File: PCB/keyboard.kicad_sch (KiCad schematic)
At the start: 0 parts

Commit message: created MCU schematic
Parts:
- added C? (x3): 0.1uF, symbol Device:C_Small
- added C? (x2): 22pF, symbol Device:C_Small
- added C?: 1uf, symbol Device:C_Small
- added C?: 10uF, symbol Device:C_Small
- added R? (x2): 10k, symbol Device:R_Small
- added R? (x2): 22, symbol Device:R_Small
- added SW?: SW_Push, symbol Switch:SW_Push
- added U?: ATmega32U4-A, Package_QFP:TQFP-44_10x10mm_P0.8mm, symbol MCU_Microchip_ATmega:ATmega32U4-A
- added Y?: 16MHz, symbol Device:Crystal_GND24_Small
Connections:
- new net: C?.2, U?.17 (XTAL1), Y?.1
- new net: R?.2, SW?.2, U?.13 (~{RESET})
- new net: C?.2, U?.16 (XTAL2), Y?.3
- new net: R?.2, U?.3 (D-)
- new net: R?.1, U?.33 (~{HWB}/PE2)
- new net: R?.2, U?.4 (D+)
- new net: C?.1, U?.6 (UCAP)
- new net +5V: C?.1, C?.1, C?.1, C?.1, R?.1, U?.14 (VCC), U?.2 (UVCC), U?.24 (AVCC), U?.34 (VCC), U?.44 (AVCC), U?.7 (VBUS)
- new net D +: R?.1
- new net D -: R?.1
- new net GND: C?.1, C?.1, C?.2, C?.2, C?.2, C?.2, C?.2, R?.2, SW?.1, U?.15 (GND), U?.23 (GND), U?.35 (GND), U?.43 (GND), U?.5 (UGND), Y?.2, Y?.4
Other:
- note added: "1"
- note added: "22/10/22"
- note added: "Smth66"

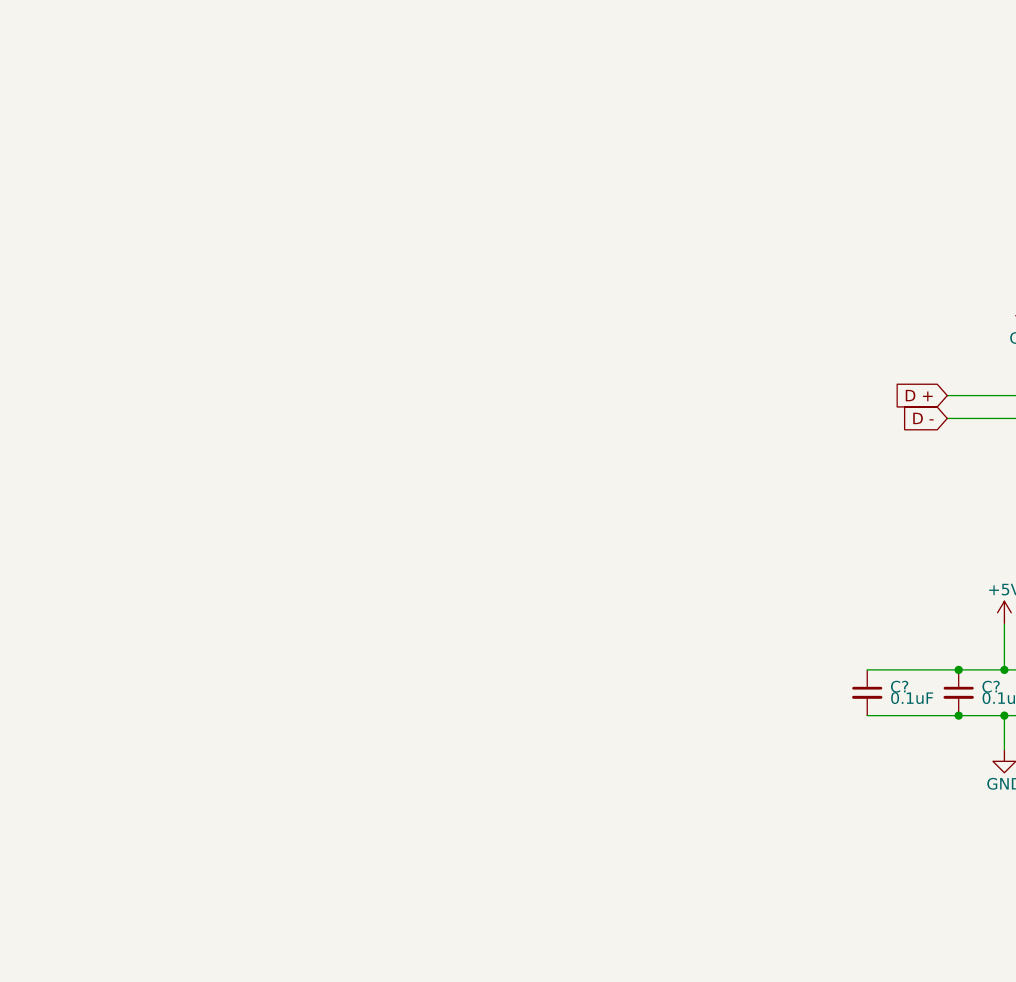
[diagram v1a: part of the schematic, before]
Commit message: added USB and Switch to schematic
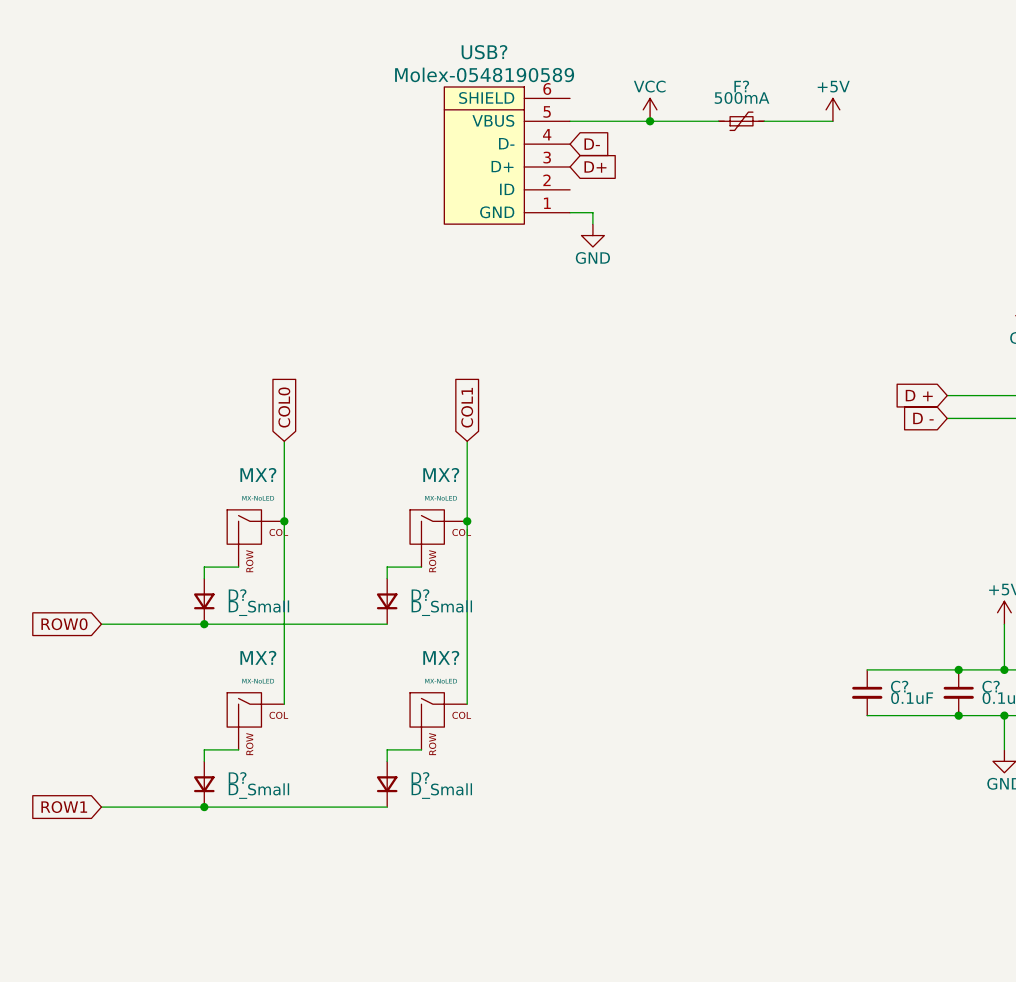
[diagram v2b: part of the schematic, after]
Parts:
- added D? (x4): D_Small, symbol Device:D_Small
- added F?: 500mA, symbol Device:Polyfuse_Small
- added MX? (x4): MX-NoLED, symbol MX_Alps_Hybrid:MX-NoLED
- added USB?: Molex-0548190589, symbol random-keyboard-parts:Molex-0548190589
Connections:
- net +5V: now also F?.2
- net GND: now also USB?.1 (GND)
- new net: D?.2 (A), MX?.2 (ROW) (x4)
- new net COL0: MX?.1 (COL), MX?.1 (COL)
- new net COL1: MX?.1 (COL), MX?.1 (COL)
- new net D+: USB?.3 (D+)
- new net D-: USB?.4 (D-)
- new net ROW0: D?.1 (K), D?.1 (K)
- new net ROW1: D?.1 (K), D?.1 (K)
- new net VCC: F?.1, USB?.5 (VBUS)

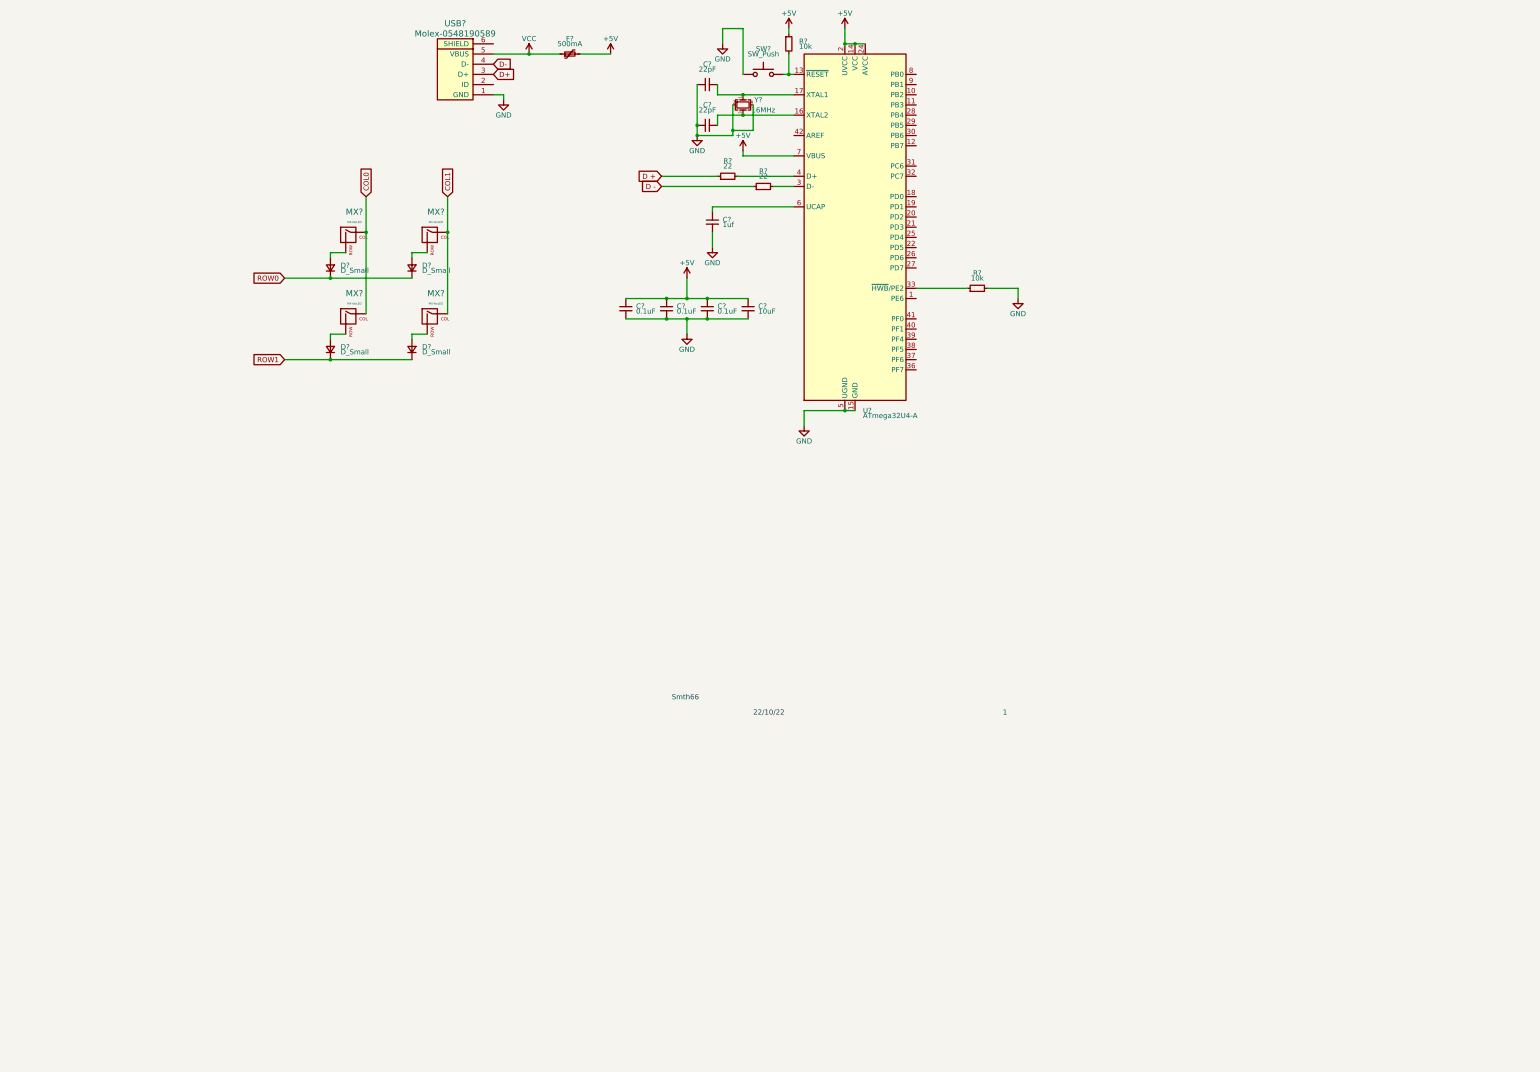
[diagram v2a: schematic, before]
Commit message: added switch grid to schematic
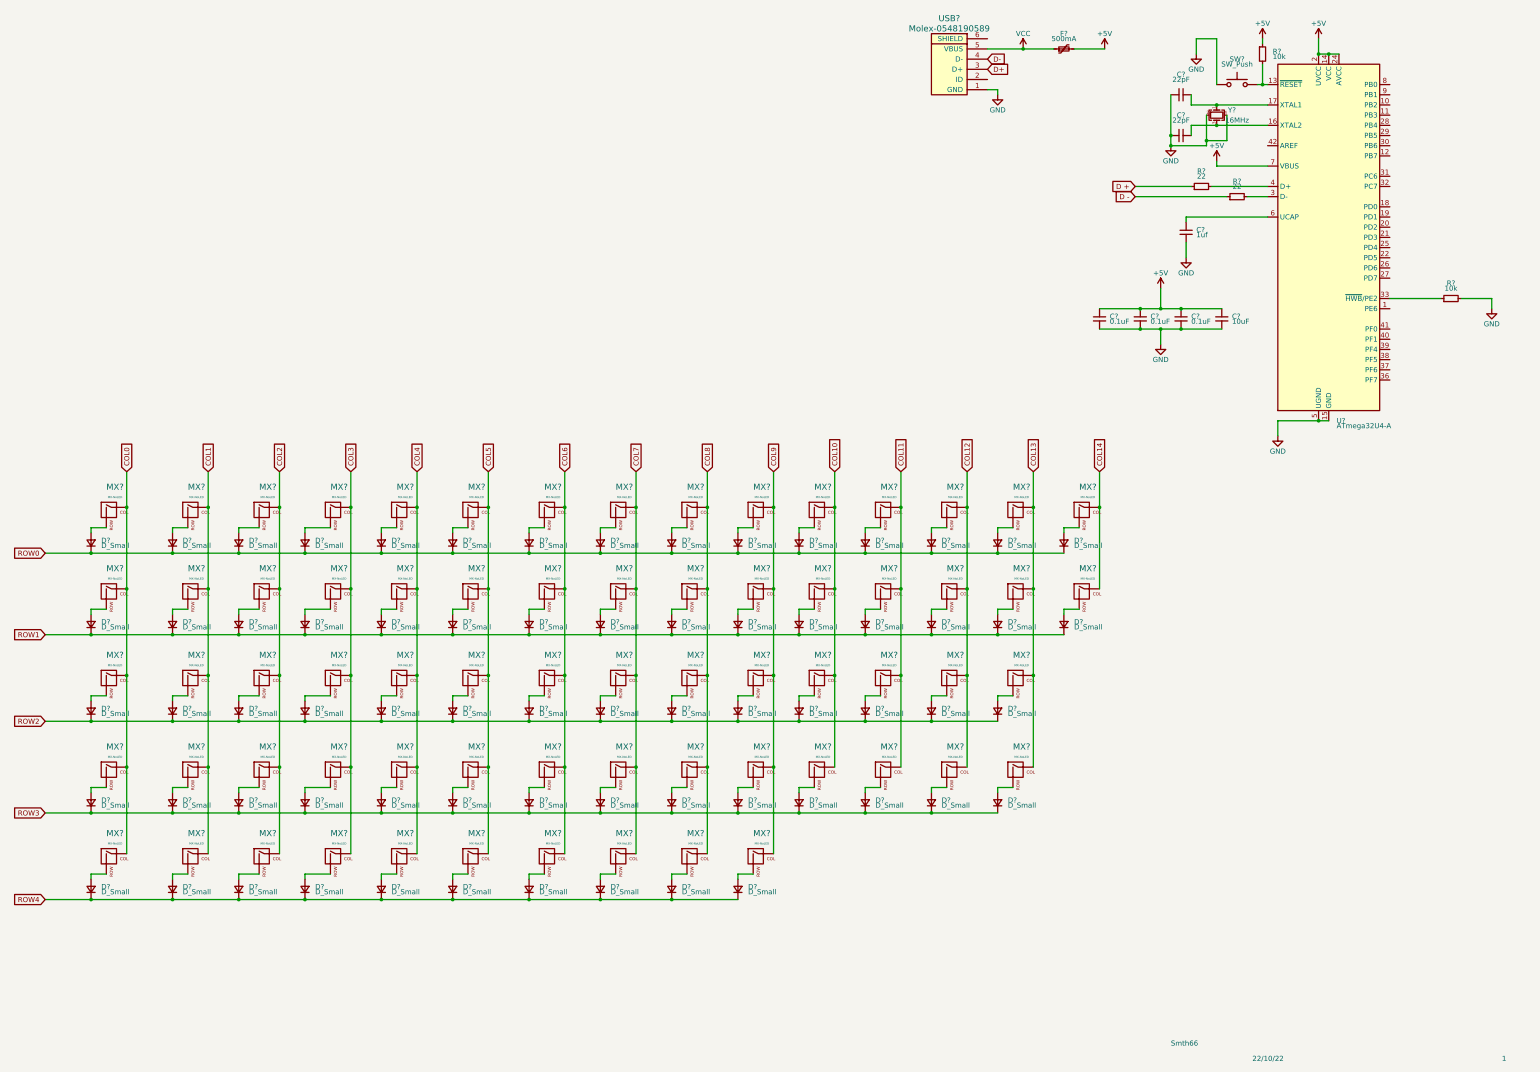
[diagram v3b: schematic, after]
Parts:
- added D? (x64): D_Small, symbol Device:D_Small
- added MX? (x64): MX-NoLED, symbol MX_Alps_Hybrid:MX-NoLED
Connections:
- net COL0: now also MX?.1 (COL), MX?.1 (COL), MX?.1 (COL)
- net COL1: now also MX?.1 (COL), MX?.1 (COL), MX?.1 (COL)
- net ROW0: now also D?.1 (K), D?.1 (K), D?.1 (K), D?.1 (K), D?.1 (K), D?.1 (K), D?.1 (K), D?.1 (K), D?.1 (K), D?.1 (K), D?.1 (K), D?.1 (K), D?.1 (K)
- net ROW1: now also D?.1 (K), D?.1 (K), D?.1 (K), D?.1 (K), D?.1 (K), D?.1 (K), D?.1 (K), D?.1 (K), D?.1 (K), D?.1 (K), D?.1 (K), D?.1 (K), D?.1 (K)
- new net: D?.2 (A), MX?.2 (ROW) (x64)
- new net COL10: MX?.1 (COL), MX?.1 (COL), MX?.1 (COL), MX?.1 (COL)
- new net COL11: MX?.1 (COL), MX?.1 (COL), MX?.1 (COL), MX?.1 (COL)
- new net COL12: MX?.1 (COL), MX?.1 (COL), MX?.1 (COL), MX?.1 (COL)
- new net COL13: MX?.1 (COL), MX?.1 (COL), MX?.1 (COL), MX?.1 (COL)
- new net COL14: MX?.1 (COL), MX?.1 (COL)
- new net COL2: MX?.1 (COL), MX?.1 (COL), MX?.1 (COL), MX?.1 (COL), MX?.1 (COL)
- new net COL3: MX?.1 (COL), MX?.1 (COL), MX?.1 (COL), MX?.1 (COL), MX?.1 (COL)
- new net COL4: MX?.1 (COL), MX?.1 (COL), MX?.1 (COL), MX?.1 (COL), MX?.1 (COL)
- new net COL5: MX?.1 (COL), MX?.1 (COL), MX?.1 (COL), MX?.1 (COL), MX?.1 (COL)
- new net COL6: MX?.1 (COL), MX?.1 (COL), MX?.1 (COL), MX?.1 (COL), MX?.1 (COL)
- new net COL7: MX?.1 (COL), MX?.1 (COL), MX?.1 (COL), MX?.1 (COL), MX?.1 (COL)
- new net COL8: MX?.1 (COL), MX?.1 (COL), MX?.1 (COL), MX?.1 (COL), MX?.1 (COL)
- new net COL9: MX?.1 (COL), MX?.1 (COL), MX?.1 (COL), MX?.1 (COL), MX?.1 (COL)
- new net ROW2: D?.1 (K), D?.1 (K), D?.1 (K), D?.1 (K), D?.1 (K), D?.1 (K), D?.1 (K), D?.1 (K), D?.1 (K), D?.1 (K), D?.1 (K), D?.1 (K), D?.1 (K), D?.1 (K)
- new net ROW3: D?.1 (K), D?.1 (K), D?.1 (K), D?.1 (K), D?.1 (K), D?.1 (K), D?.1 (K), D?.1 (K), D?.1 (K), D?.1 (K), D?.1 (K), D?.1 (K), D?.1 (K), D?.1 (K)
- new net ROW4: D?.1 (K), D?.1 (K), D?.1 (K), D?.1 (K), D?.1 (K), D?.1 (K), D?.1 (K), D?.1 (K), D?.1 (K), D?.1 (K)
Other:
- moved on the sheet: C?, D?, F?, MX?, R?, SW?, U?, USB?, Y?

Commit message: Finnished Schematic????
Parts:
- C1, C2, C3, C4, C5, C6, C7: renamed from C?; footprint (none) -> Capacitor_SMD:C_0805_2012Metric
- D1, D10, D11, D12, D13, D14, D15, D16, D17, D18, D19, D2, D20, D21, D22, D23, D24, D25, D26, D27, D28, D29, D3, D30, D31, D32, D33, D34, D35, D36, D37, D38, D39, D4, D40, D41, D42, D43, D44, D45, D46, D47, D48, D49, D5, D50, D51, D52, D53, D54, D55, D56, D57, D58, D59, D6, D60, D61, D62, D63, D64, D65, D66, D67, D68, D7, D8, D9: renamed from D?; footprint (none) -> Diode_SMD:D_SOD-123
- F1: renamed from F?; footprint (none) -> Fuse:Fuse_1206_3216Metric
- MX1, MX10, MX11, MX12, MX13, MX14, MX15, MX16, MX17, MX18, MX19, MX2, MX20, MX21, MX22, MX23, MX24, MX25, MX26, MX27, MX28, MX29, MX3, MX30, MX31, MX32, MX33, MX34, MX35, MX36, MX37, MX38, MX39, MX4, MX40, MX41, MX42, MX43, MX44, MX45, MX46, MX47, MX48, MX49, MX5, MX50, MX51, MX52, MX53, MX54, MX55, MX56, MX57, MX58, MX59, MX6, MX60, MX61, MX62, MX63, MX64, MX65, MX66, MX67, MX68, MX7, MX8, MX9: renamed from MX?; footprint (none) -> MX_Alps_Hybrid:MX-1U-NoLED
- R1, R2, R3, R4: renamed from R?; footprint (none) -> Resistor_SMD:R_0805_2012Metric
- SW1: renamed from SW?; footprint (none) -> random-keyboard-parts:SKQG-1155865
- USB1: renamed from USB?; footprint (none) -> random-keyboard-parts:Molex-0548190589
- Y1: renamed from Y?; footprint (none) -> Crystal:Crystal_SMD_3225-4Pin_3.2x2.5mm
- gave numbers to parts that had none: 1
